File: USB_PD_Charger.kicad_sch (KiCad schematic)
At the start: 39 parts, among them J9 Conn_01x05, Q1 AON7403, U1 LM3489QMM/NOPB, U2 TPS65987DDHRSHR, U3 MX25L8006EM1I-12G

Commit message: Replaced 12.4k resistor with two basic parts
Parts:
- L1: LCSC (none) -> C351119
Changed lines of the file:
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@@
+			)
+		)
+		(property "LCSC" "C351119"
+			(at 184.15 33.02 90)
+			(effects
+				(font
+					(size 1.27 1.27)
+				)
+				(hide yes)
 			)
 		)

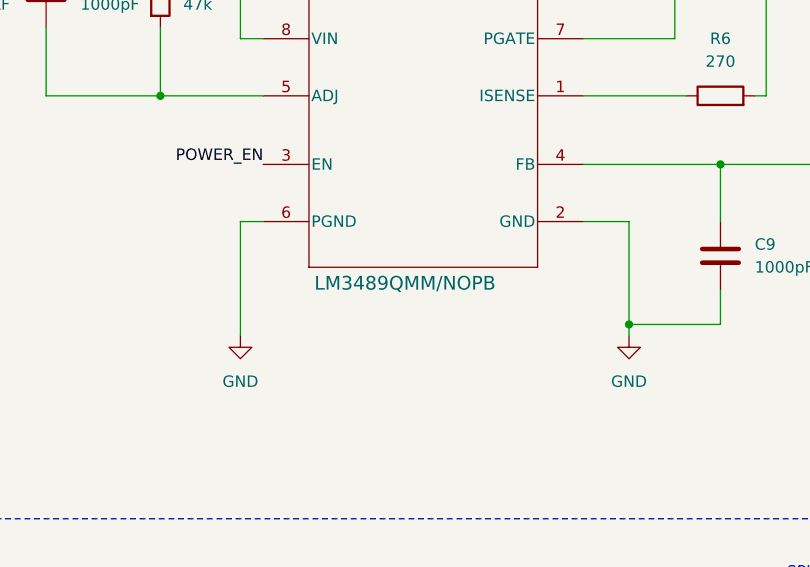
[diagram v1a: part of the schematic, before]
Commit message: Increased inductor size
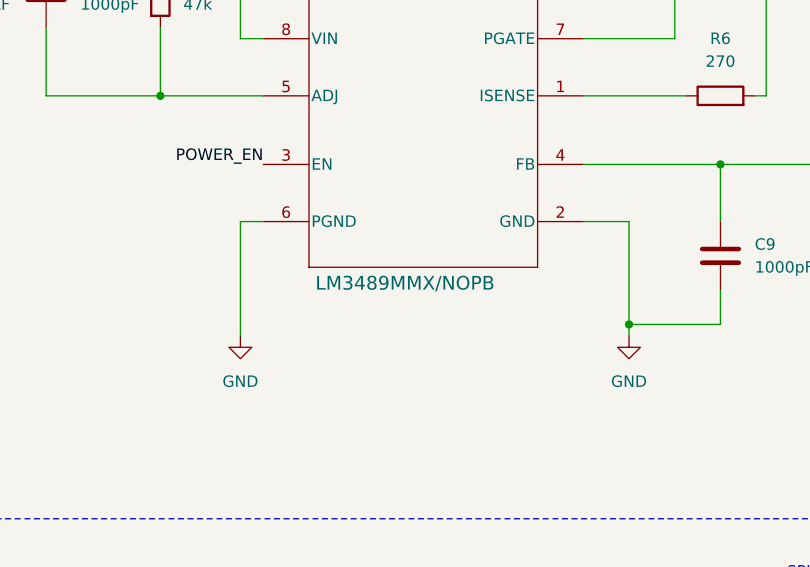
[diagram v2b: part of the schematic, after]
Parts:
- L1: LCSC C351119 -> C2880077; Part_Number YSPI0730-100M -> TMPA0605S-100MN-D
- U1: value LM3489QMM/NOPB -> LM3489MMX/NOPB; LCSC C2862414 -> C529297; Part_Number LM3489QMM/NOPB -> LM3489MMX/NOPB

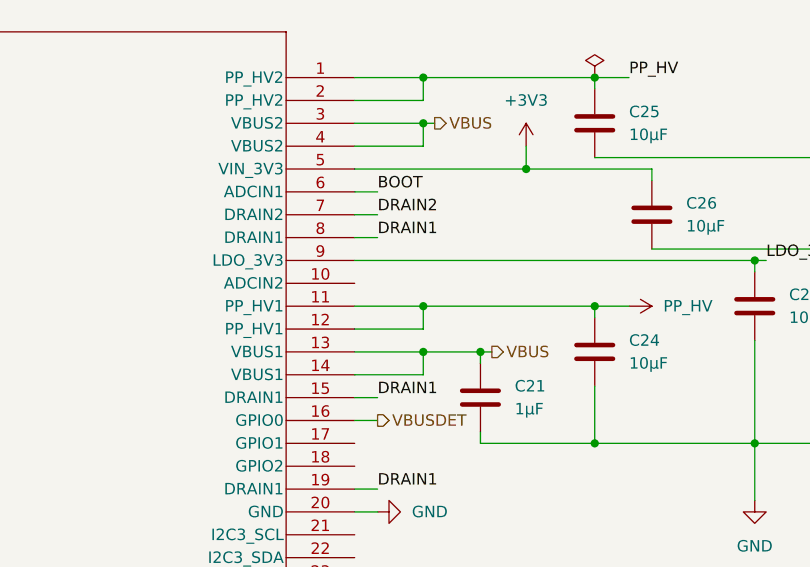
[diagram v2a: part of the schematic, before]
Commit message: Fixed USB Hub wrong net 1V0 -> 3V3
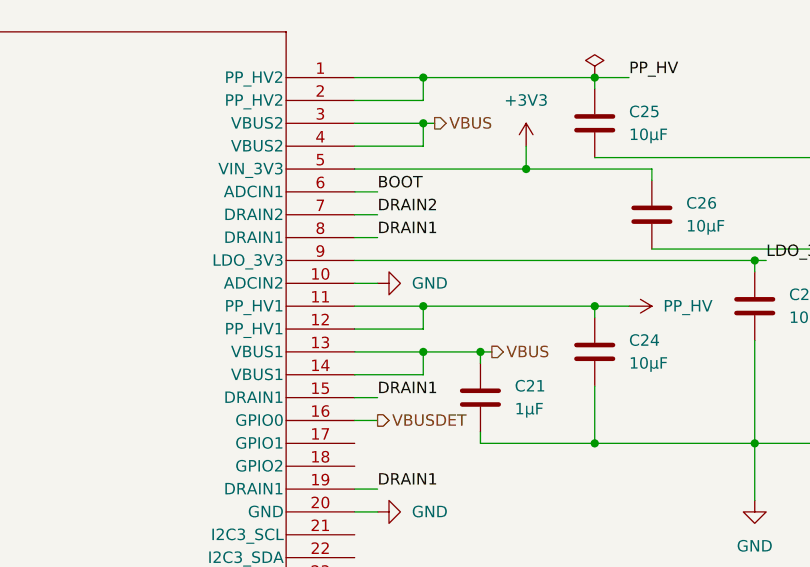
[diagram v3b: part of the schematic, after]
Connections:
- net GND: now also U2.10 (ADCIN2)
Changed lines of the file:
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@@
 	(wire
 		(pts
+			(xy 109.22 133.35) (xy 111.76 133.35)
+		)
+		(stroke
+			(width 0)
+			(type default)
+		)
+	)
+	(wire
+		(pts
 			(xy 53.34 171.45) (xy 21.59 171.45)
 		)
@@
 					(unit 1)
 				)
+			)
+		)
+	)
+	(symbol
+		(lib_id "power:GND")
+		(at 111.76 133.35 90)
+		(unit 1)
+		(exclude_from_sim no)
+		(in_bom yes)
+		(on_board yes)
+		(dnp no)
+		(fields_autoplaced yes)
+		(property "Reference" "#PWR0101"
+			(at 118.11 133.35 0)
+			(effects
+				(font
+					(size 1.27 1.27)
+				)
+				(hide yes)
+			)
+		)
+		(property "Value" "GND"
+			(at 115.57 133.3499 90)
+			(effects
+				(font
+					(size 1.27 1.27)
+				)
+				(justify right)
+			)
+		)
+		(property "Footprint" ""
+			(at 111.76 133.35 0)
+			(effects
+				(font
+					(size 1.27 1.27)
+				)
+				(hide yes)
+			)
+		)
+		(property "Datasheet" ""
+			(at 111.76 133.35 0)
+			(effects
+				(font
+					(size 1.27 1.27)
+				)
+				(hide yes)
+			)
+		)
+		(property "Description" "Power symbol creates a global label with name \"GND\" , ground"
+			(at 111.76 133.35 0)
+			(effects
+				(font
+					(size 1.27 1.27)
+				)
+				(hide yes)
+			)
+		)
+		(pin "1"
+		)
+		(instances
+			(project "XG_Mobile_Dock"
+				(path "/f97e6956-ab08-42cb-8fed-03fa58e87f0e/fa35204a-fbf7-48de-bc5b-11fc2e29f675"
+					(reference "#PWR0101")
+					(unit 1)
+				)

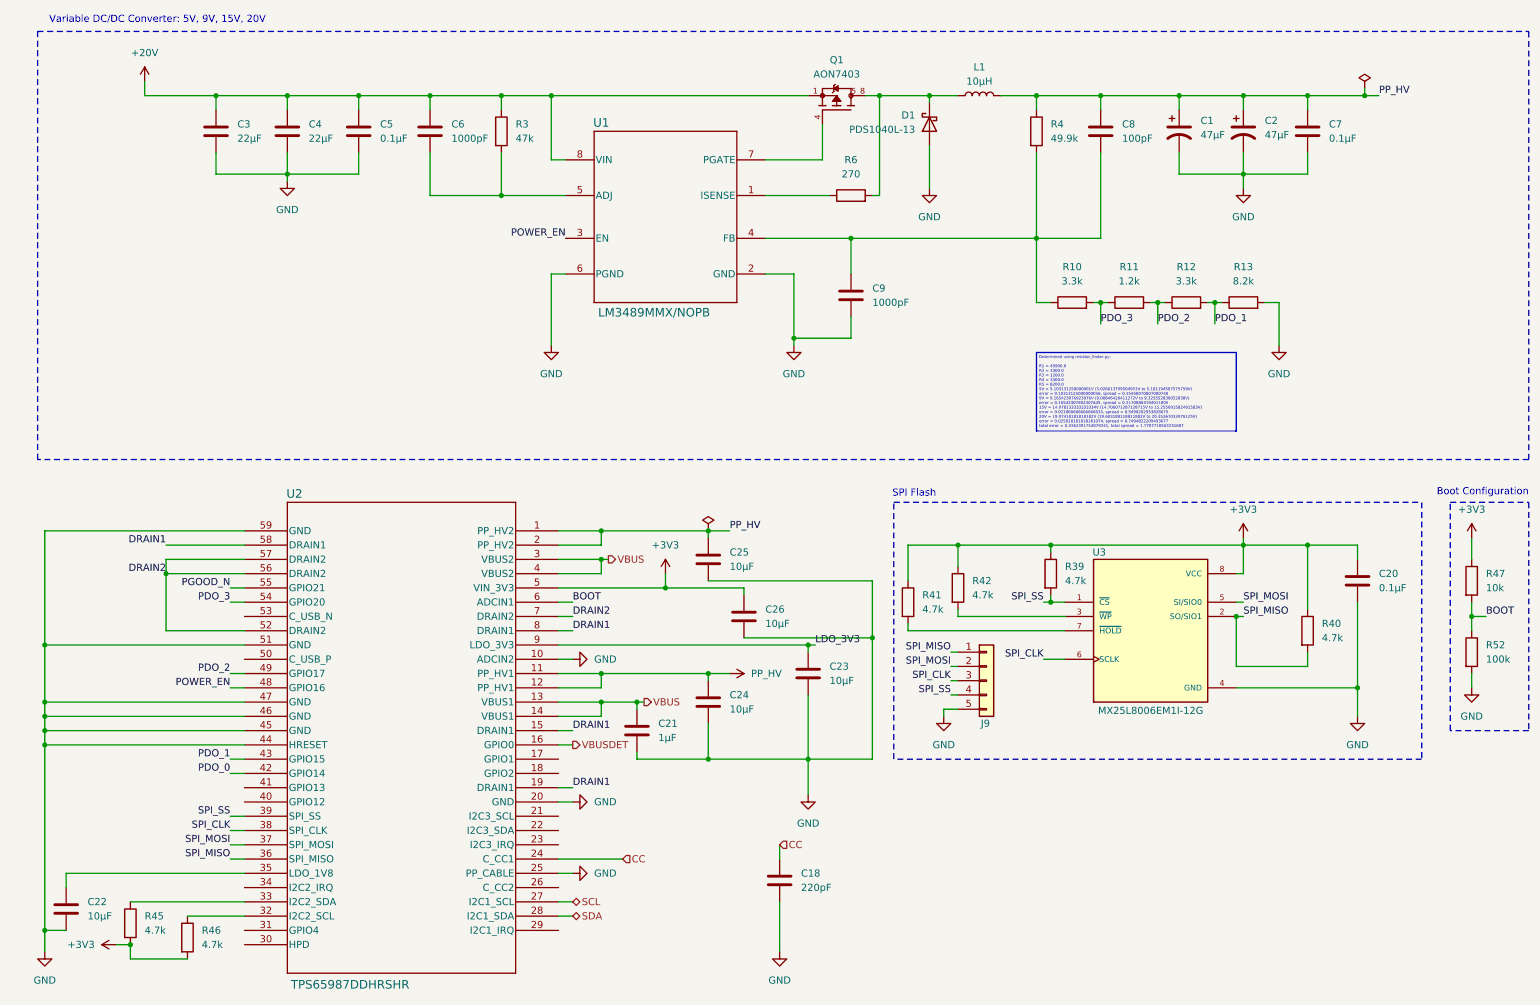
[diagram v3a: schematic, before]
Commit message: Improvements to board
* Break up power switch into input and output signals
* Removed POWER_EN from USB PD charger (GPIO does not work due to one event per pin)
* Added MOSFET to buffer GPIO output from PD IC
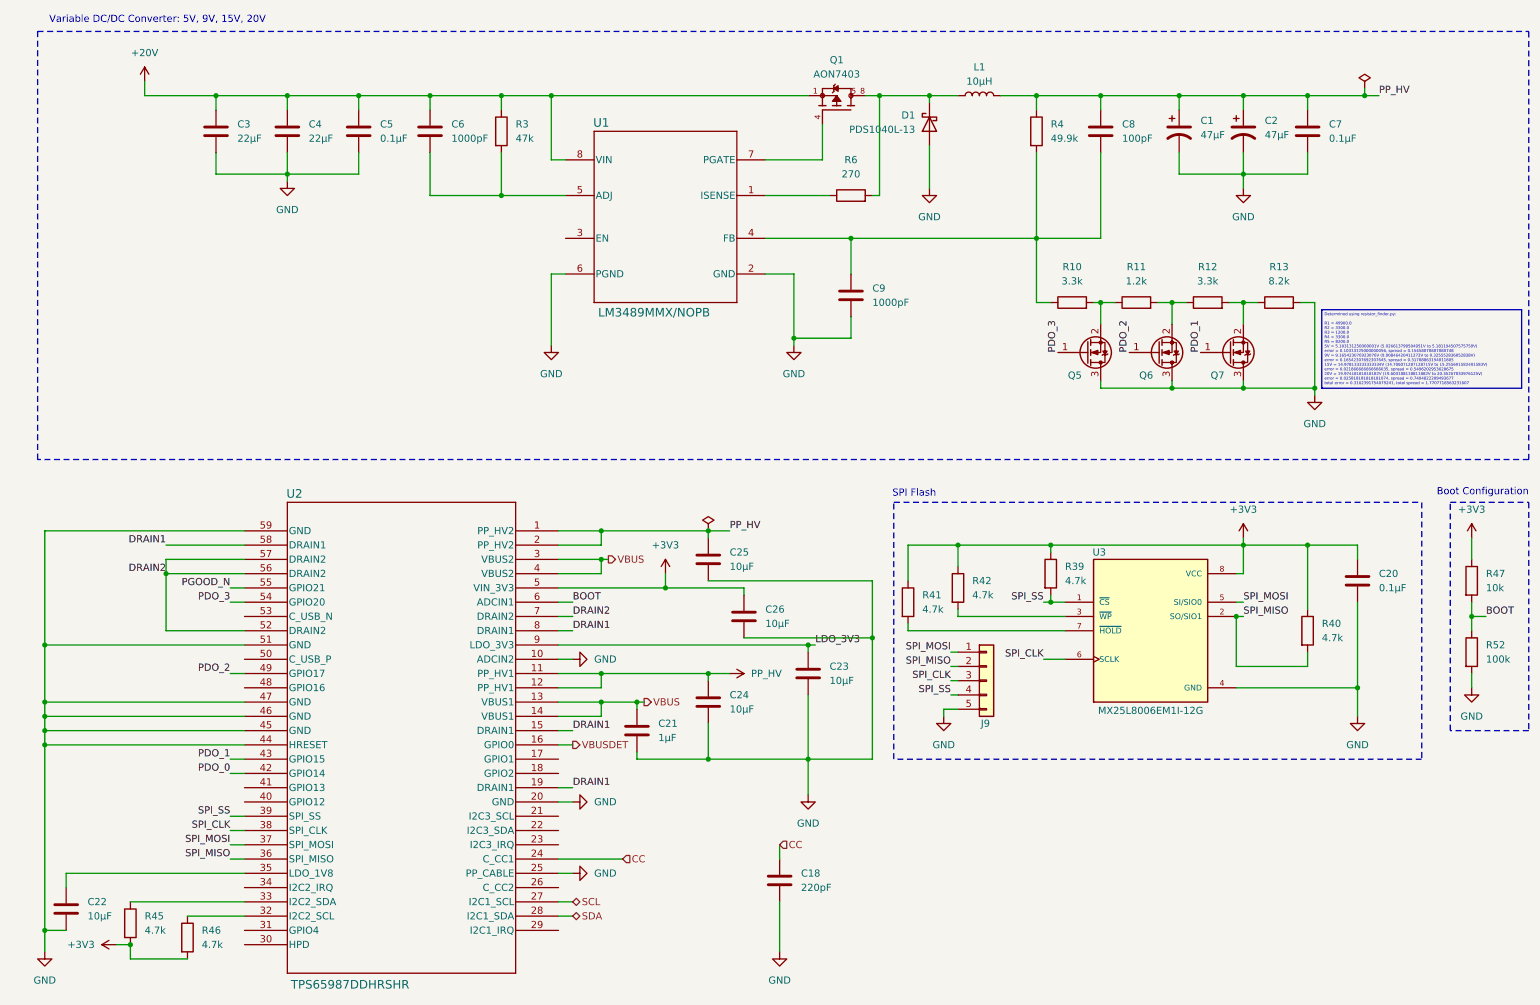
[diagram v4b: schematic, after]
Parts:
- added Q5, Q6, Q7: 2N7002W, 2N7002W:SOT-323-3_L2.0-W1.3-P1.30-LS2.1-BR, symbol Transistor_FET:BSS214NW
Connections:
- net GND: now also Q5.3 (D), Q6.3 (D), Q7.3 (D)
- net PDO_1: now also Q7.1 (G); no longer R12.2, R13.1
- net PDO_2: now also Q6.1 (G); no longer R11.2, R12.1
- net PDO_3: now also Q5.1 (G); no longer R10.2, R11.1
- net SPI_MISO: now also J9.2 (Pin_2); no longer J9.1 (Pin_1)
- net SPI_MOSI: now also J9.1 (Pin_1); no longer J9.2 (Pin_2)
- net POWER_EN: no longer names the net of U1.3 (EN)
- net POWER_EN: no longer U2.48 (GPIO16)
- new net: Q5.2 (S), R10.2, R11.1
- new net: Q6.2 (S), R11.2, R12.1
- new net: Q7.2 (S), R12.2, R13.1
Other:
- moved on the sheet: R11, R12, R13

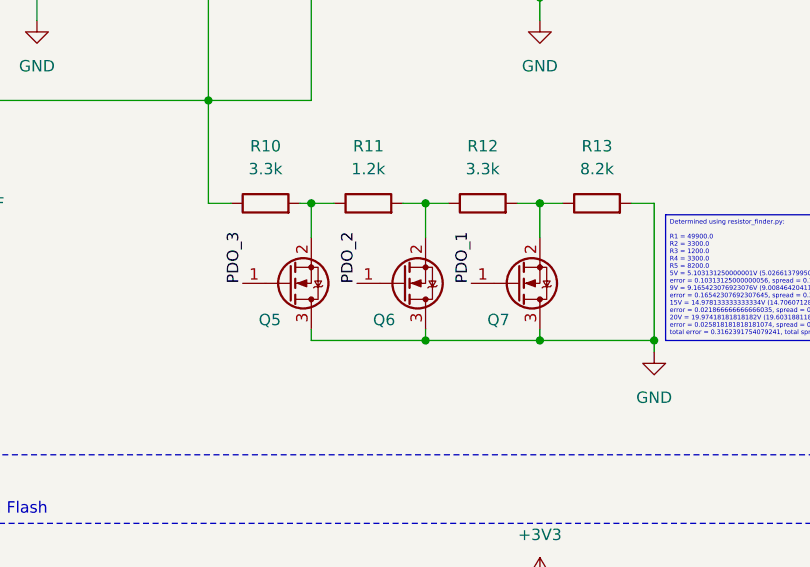
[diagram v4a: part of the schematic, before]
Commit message: Fix flipped MOSFETs for PDO signals
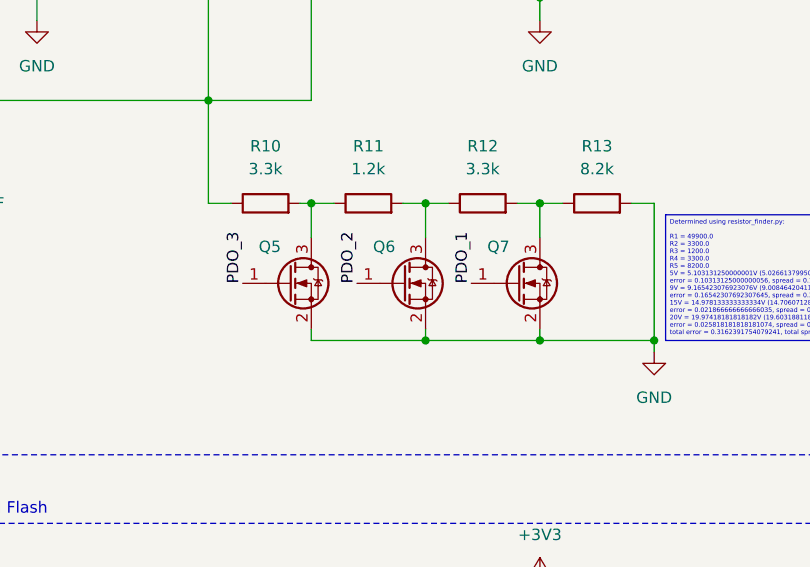
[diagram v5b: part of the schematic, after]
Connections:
- net GND: now also Q5.2 (S), Q6.2 (S), Q7.2 (S); no longer Q5.3 (D), Q6.3 (D), Q7.3 (D)
- net at R10.2, R11.1: now also Q5.3 (D); no longer Q5.2 (S)
- net at R11.2, R12.1: now also Q6.3 (D); no longer Q6.2 (S)
- net at R12.2, R13.1: now also Q7.3 (D); no longer Q7.2 (S)
